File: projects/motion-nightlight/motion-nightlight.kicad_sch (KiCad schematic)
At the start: 19 parts, among them Q1 DARK_NPN_EBC, Q2 LED_CONTROL_NPN, SW1 SW_Push, SW2 SENSOR, SW3 MODE, U1 74HC14, U2 74LS08

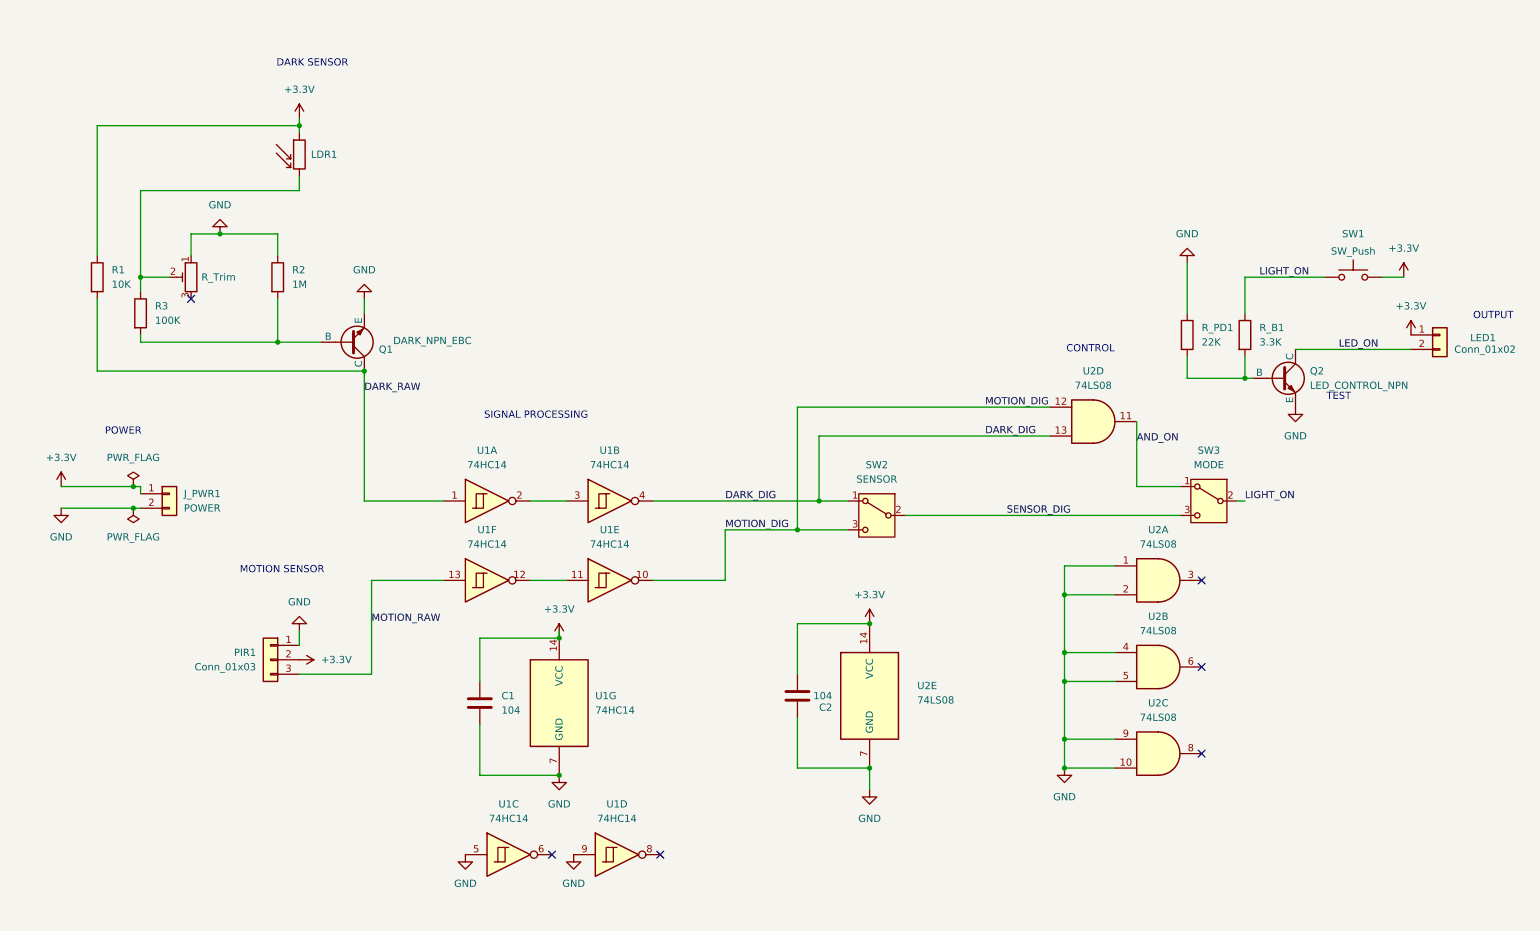
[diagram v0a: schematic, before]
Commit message: add motion off delay
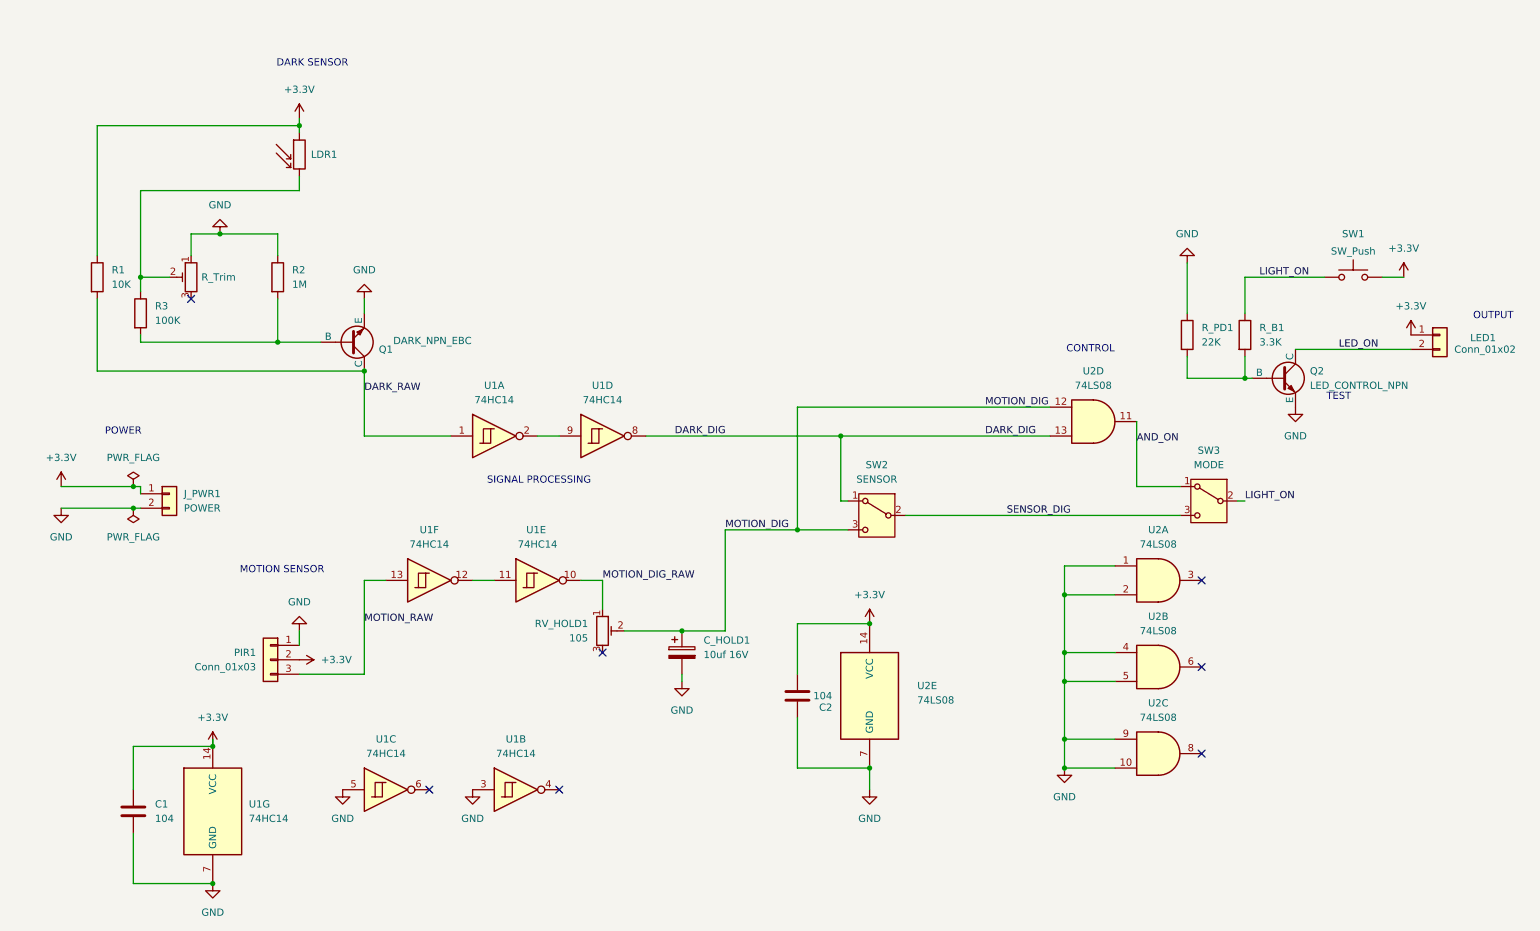
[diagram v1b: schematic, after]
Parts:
- added C_HOLD1: 10uf 16V, Capacitor_THT:C_Radial_D4.0mm_H5.0mm_P1.50mm, symbol Device:C_Polarized
- added RV_HOLD1: 105, Potentiometer_THT:Potentiometer_Runtron_RM-065_Vertical, symbol Device:R_Potentiometer_Trim
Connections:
- net DARK_DIG: now also U1.8; no longer U1.4
- net GND: now also U1.3, C_HOLD1.2; no longer U1.9
- net MOTION_DIG: now also C_HOLD1.1, RV_HOLD1.2; no longer U1.10
- net at U1.2: now also U1.9; no longer U1.3
- new net MOTION_DIG_RAW: RV_HOLD1.1, U1.10
- no-connect marks 6 -> 7
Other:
- moved on the sheet: C1, U1A, U1B, U1C, U1D, U1E, U1F, U1G

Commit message: adding motion off delay
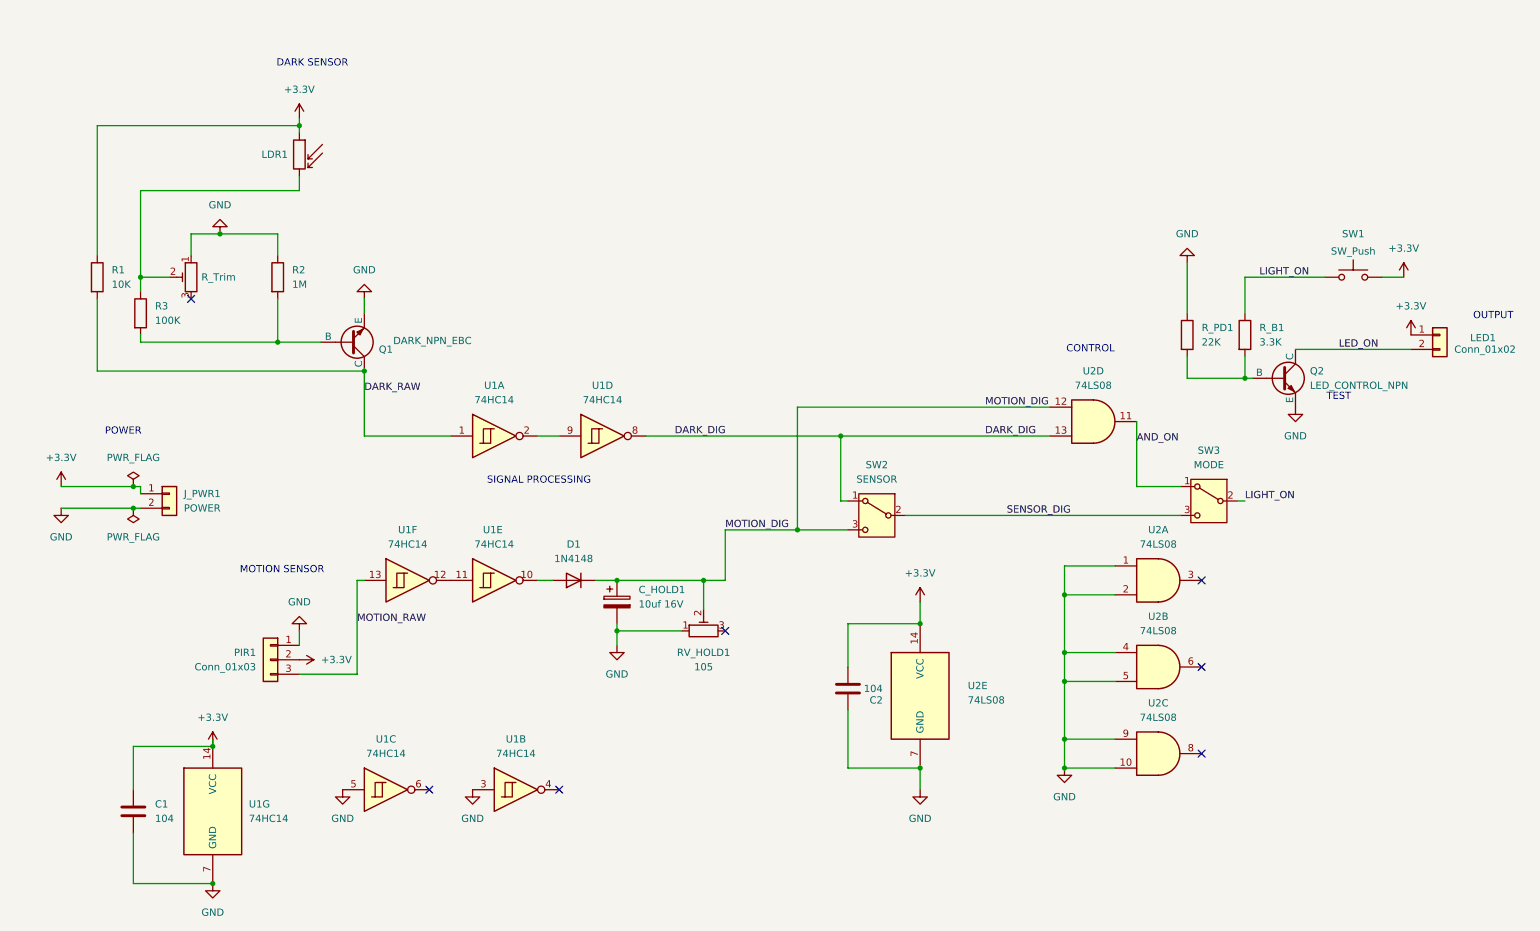
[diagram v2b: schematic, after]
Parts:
- added D1: 1N4148, Diode_THT:D_DO-35_SOD27_P7.62mm_Horizontal, symbol Diode:1N4148
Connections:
- net GND: now also RV_HOLD1.1
- net MOTION_DIG: now also D1.1 (K)
- net MOTION_DIG_RAW: no longer names the net of U1.10
- net MOTION_DIG_RAW: now also D1.2 (A); no longer RV_HOLD1.1
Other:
- moved on the sheet: C2, C_HOLD1, LDR1, RV_HOLD1, U1E, U1F, U2E

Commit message: fix up footprints and add step for trim pots
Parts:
- C_HOLD1: value 10uf 16V -> 10uf
- J_PWR1: value POWER -> - POWER +; footprint TerminalBlock_Altech:Altech_AK100_1x02_P5.00mm -> TerminalBlock_Phoenix:TerminalBlock_Phoenix_PT-1,5-2-3.5-H_1x02_P3.50mm_Horizontal
- LED1: value Conn_01x02 -> LED
- PIR1: value Conn_01x03 -> PIR
- Q1: value DARK_NPN_EBC -> DARK ON
- Q2: value LED_CONTROL_NPN -> LED ON
- RV1: value R_Trim -> DARK TRIM; footprint Potentiometer_THT:Potentiometer_Bourns_3296W_Vertical -> Potentiometer_THT:Potentiometer_Runtron_RM-065_Vertical
- RV_HOLD1: value 105 -> MOTION TRIM
- SW1: value SW_Push -> LAMP TEST
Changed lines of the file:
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@@
 			)
 		)
-		(property "Value" "10uf 16V"
+		(property "Value" "10uf"
 			(at 125.73 121.0309 0)
 			(effects
@@
 			)
 		)
-		(property "Value" "POWER"
+		(property "Value" "- POWER +"
 			(at 45.72 104.1399 0)
 			(effects
@@
 			)
 		)
-		(property "Footprint" "TerminalBlock_Altech:Altech_AK100_1x02_P5.00mm"
+		(property "Footprint" "TerminalBlock_Phoenix:TerminalBlock_Phoenix_PT-1,5-2-3.5-H_1x02_P3.50mm_Horizontal"
 			(at 43.18 101.6 0)
 			(effects
@@
 			)
 		)
-		(property "Value" "SW_Push"
+		(property "Value" "LAMP TEST"
 			(at 251.46 58.928 0)
 			(effects
@@
 			)
 		)
-		(property "Value" "Conn_01x03"
+		(property "Value" "PIR"
 			(at 58.42 132.0799 0)
 			(effects
@@
 			)
 		)
-		(property "Value" "105"
+		(property "Value" "MOTION TRIM"
 			(at 137.16 132.08 90)
 			(effects
@@
 			)
 		)
-		(property "Value" "Conn_01x02"
+		(property "Value" "LED"
 			(at 269.24 76.1999 0)
 			(effects
@@
 			)
 		)
-		(property "Value" "DARK_NPN_EBC"
+		(property "Value" "DARK ON"
 			(at 82.55 74.676 0)
 			(effects
@@
 			)
 		)
-		(property "Value" "R_Trim"
+		(property "Value" "DARK TRIM"
 			(at 51.816 63.5 0)
 			(effects
@@
 			)
 		)
-		(property "Footprint" "Potentiometer_THT:Potentiometer_Bourns_3296W_Vertical"
+		(property "Footprint" "Potentiometer_THT:Potentiometer_Runtron_RM-065_Vertical"
 			(at 46.99 63.5 0)
 			(effects
@@
 			)
 		)
-		(property "Value" "LED_CONTROL_NPN"
+		(property "Value" "LED ON"
 			(at 243.84 82.5499 0)
 			(effects

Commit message: final THT version
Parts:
- added J1: J_PWR3, symbol Connector:Conn_01x03_Socket
- added LED2: LED, Connector_JST:JST_XH_B2B-XH-A_1x02_P2.50mm_Vertical, symbol Connector_Generic:Conn_01x02
- U2: value 74LS08 -> 74HC08
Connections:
- net GND: now also J1.2 (Pin_2); no longer U1.3, U1.5
- net LED_ON: now also LED2.2 (Pin_2)
- net MOTION_DIG: now also U1.3; no longer SW2.3 (C)
- net MOTION_DIG_BUF: now reaches U1.6
- net MOTION_DIG_BUF: now also SW2.3 (C)
- net at U1.4: now also U1.5
- net +3.3V renamed V_CONTROL
- net V_CONTROL: now also J1.1 (Pin_1)
- new net V_LED: J1.3 (Pin_3), LED2.1 (Pin_1)
- no-connect marks 7 -> 5
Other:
- moved on the sheet: C2, J_PWR1, LDR1, LED1, Q1, Q2, R1, R2, R3, R_B1, R_PD1, SW1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

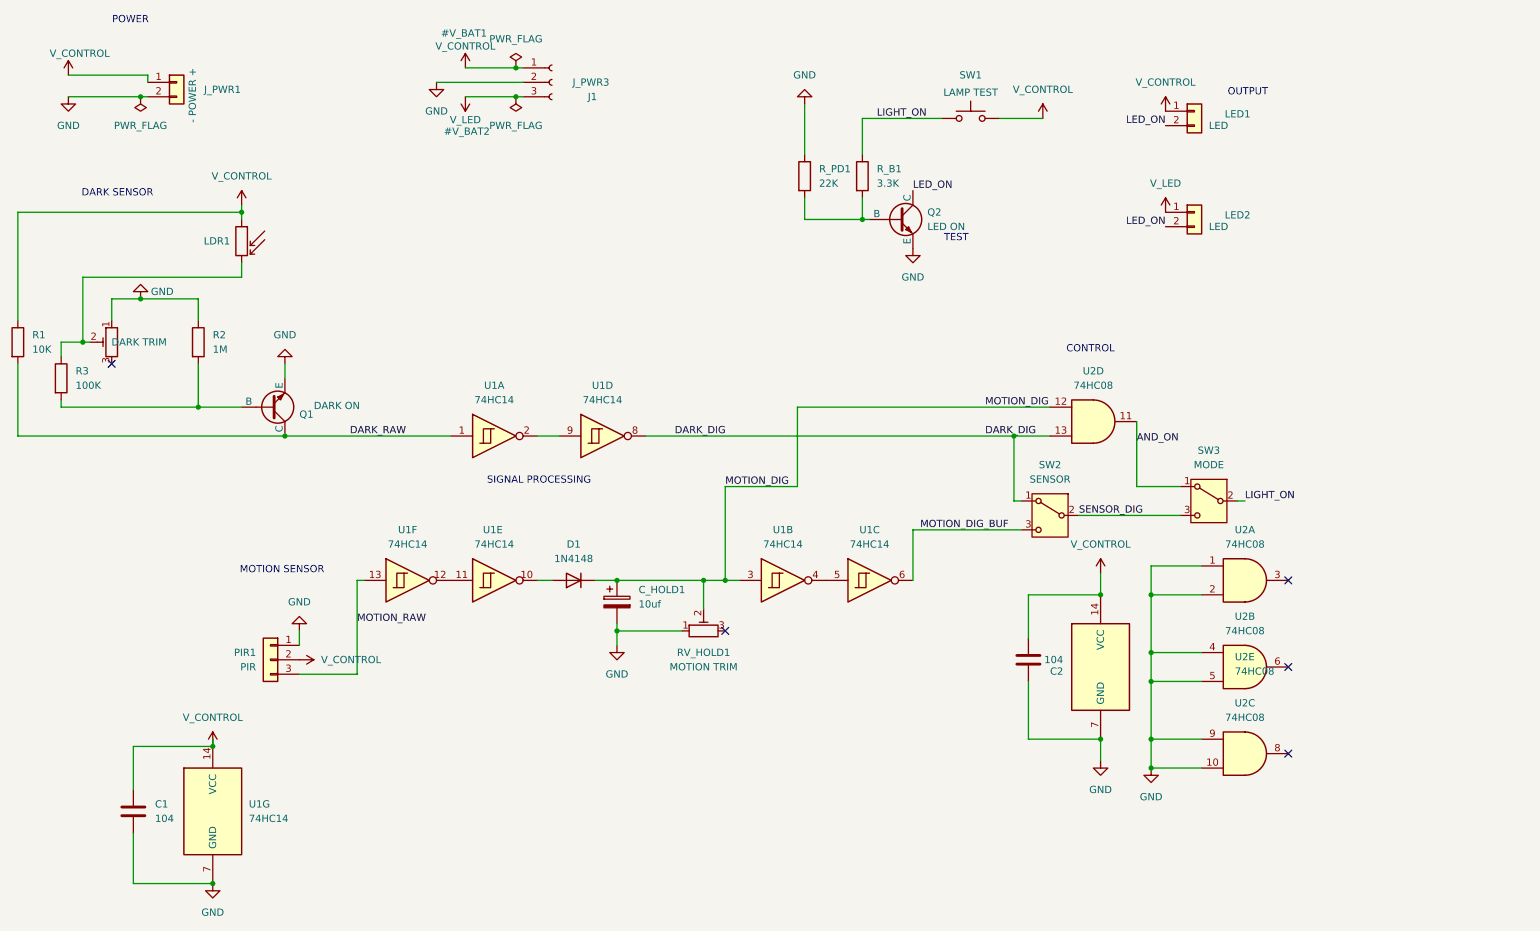
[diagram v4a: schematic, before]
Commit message: SMD version ready for fab
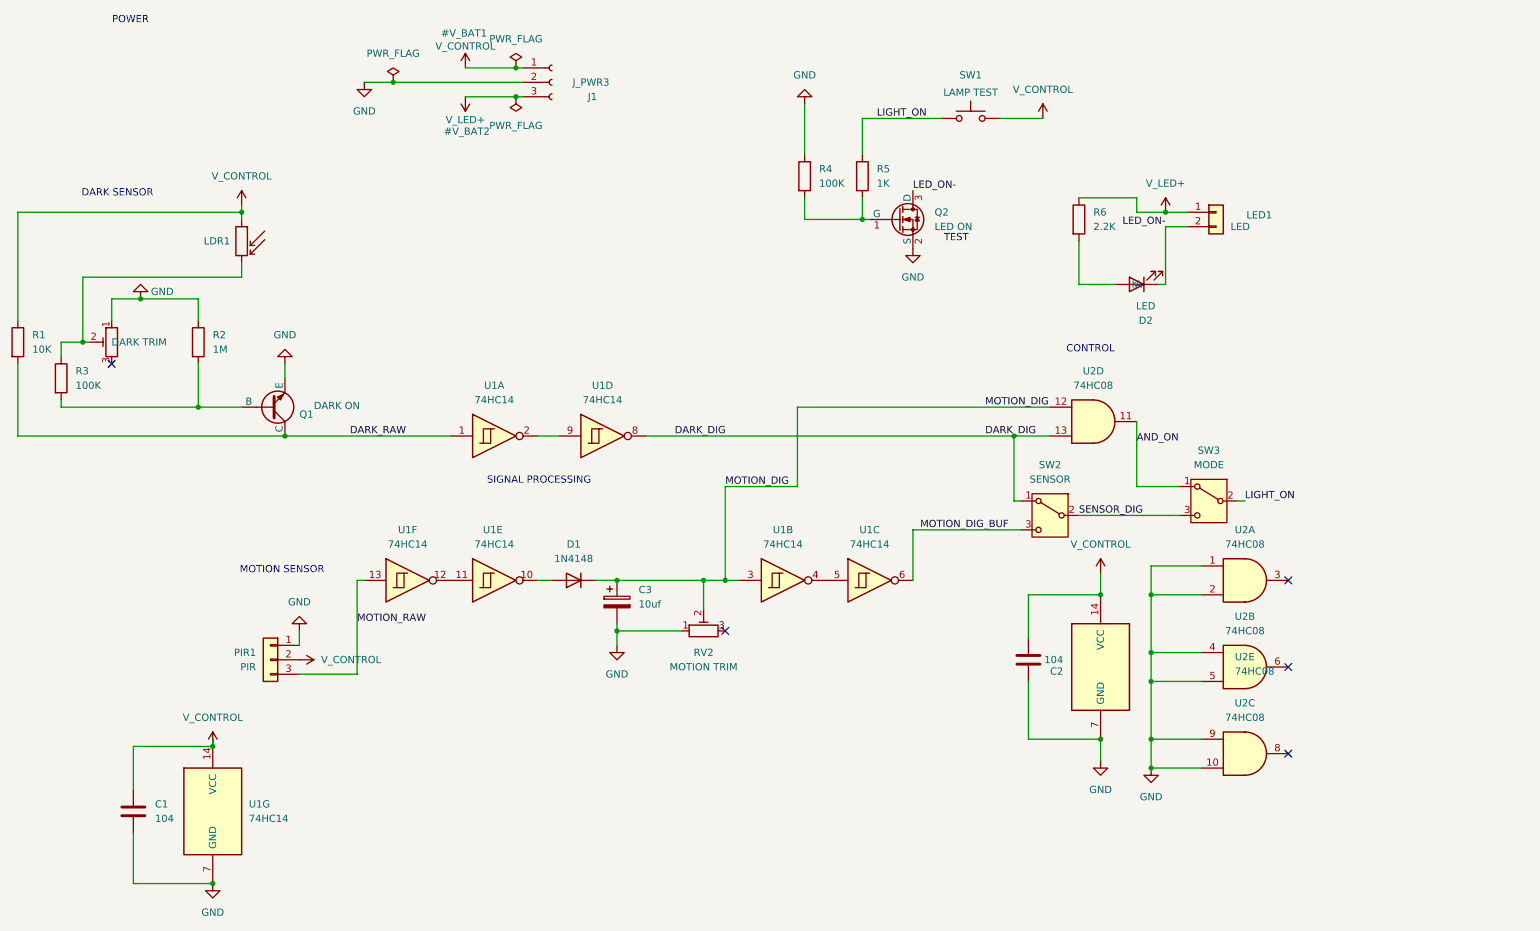
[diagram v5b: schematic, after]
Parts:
- removed J_PWR1: - POWER +, TerminalBlock_Phoenix:TerminalBlock_Phoenix_PT-1,5-2-3.5-H_1x02_P3.50mm_Horizontal, symbol Connector_Generic:Conn_01x02
- removed LED1: LED, Connector_JST:JST_XH_B2B-XH-A_1x02_P2.50mm_Vertical, symbol Connector_Generic:Conn_01x02
- added D2: LED, LED_SMD:LED_0805_2012Metric, symbol Device:LED
- added R6: 2.2K, Resistor_SMD:R_0805_2012Metric_Pad1.20x1.40mm_HandSolder, symbol Device:R
- C1, C2: footprint Capacitor_THT:C_Disc_D3.0mm_W2.0mm_P2.50mm -> Capacitor_SMD:C_0805_2012Metric_Pad1.18x1.45mm_HandSolder
- C3: renamed from C_HOLD1; footprint Capacitor_THT:C_Radial_D4.0mm_H5.0mm_P1.50mm -> Capacitor_SMD:C_0805_2012Metric_Pad1.18x1.45mm_HandSolder
- D1: footprint Diode_THT:D_DO-35_SOD27_P7.62mm_Horizontal -> Diode_SMD:D_SOD-123
- J1: footprint (none) -> Connector_JST:JST_XH_B3B-XH-A_1x03_P2.50mm_Vertical
- Q1: footprint Package_TO_SOT_THT:TO-92_Inline -> Package_TO_SOT_SMD:SOT-23_Handsoldering
- Q2: footprint Package_TO_SOT_THT:TO-92_Inline -> Package_TO_SOT_SMD:SOT-23_Handsoldering; symbol Transistor_BJT:Q_NPN_EBC -> Transistor_FET:Q_NMOS_GSD
- R1, R2, R3: footprint Resistor_THT:R_Axial_DIN0207_L6.3mm_D2.5mm_P7.62mm_Horizontal -> Resistor_SMD:R_0805_2012Metric_Pad1.20x1.40mm_HandSolder
- R4: renamed from R_PD1; value 22K -> 100K; footprint Resistor_THT:R_Axial_DIN0207_L6.3mm_D2.5mm_P7.62mm_Horizontal -> Resistor_SMD:R_0805_2012Metric_Pad1.20x1.40mm_HandSolder
- R5: renamed from R_B1; value 3.3K -> 1K; footprint Resistor_THT:R_Axial_DIN0207_L6.3mm_D2.5mm_P7.62mm_Horizontal -> Resistor_SMD:R_0805_2012Metric_Pad1.20x1.40mm_HandSolder
- RV1: footprint Potentiometer_THT:Potentiometer_Runtron_RM-065_Vertical -> Potentiometer_SMD:Potentiometer_Bourns_TC33X_Vertical
- RV2: renamed from RV_HOLD1; footprint Potentiometer_THT:Potentiometer_Runtron_RM-065_Vertical -> Potentiometer_SMD:Potentiometer_Bourns_TC33X_Vertical
- SW2, SW3: footprint Longracks:SW_Slide_SPDT_3pin_2.54mm -> Button_Switch_SMD:SW_SPDT_PCM12
- U1, U2: footprint Package_DIP:DIP-14_W7.62mm -> Package_SO:SOIC-14_3.9x8.7mm_P1.27mm
- renumbered LED2 to LED1
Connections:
- net GND: now also Q2.2 (S); no longer Q2.1 (E)
- net at R4.2, R5.2: now also Q2.1 (G); no longer Q2.2 (B)
- net LED_ON renamed LED_ON-
- net LED_ON-: now also D2.1 (K)
- net V_LED renamed V_LED+
- net V_LED+: now also R6.1
- new net: D2.2 (A), R6.2
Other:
- note removed: "OUTPUT"
- moved on the sheet: LED1
